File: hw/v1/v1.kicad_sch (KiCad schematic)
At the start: 0 parts

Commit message: Draw schematic for module V1
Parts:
- added J1: Expansion Output, symbol Connector:Conn_01x05_Socket
- added J2: Expansion Input, symbol Connector:Conn_01x05_Pin
- added U1, U2, U3: Common Anode, Display_7Segment:CA56-12CGKWA, symbol Display_Character:CA56-12CGKWA
- added U4, U5, U6: 74HC595, symbol 74xx:74HC595
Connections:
- new net: U5.9 (QH'), U6.14 (SER)
- new net: U4.9 (QH'), U5.14 (SER)
- new net +5V: J1.1 (Pin_1), J2.1 (Pin_1), U4.10 (~{SRCLR}), U4.16 (VCC), U5.10 (~{SRCLR}), U5.16 (VCC), U6.10 (~{SRCLR}), U6.16 (VCC)
- new net CLOCK: J1.3 (Pin_3), J2.3 (Pin_3), U4.11 (SRCLK), U5.11 (SRCLK), U6.11 (SRCLK)
- new net D1_SEG1: U1.12 (CA1)
- new net D1_SEG2: U1.9 (CA2)
- new net D1_SEG3: U1.8 (CA3), U5.2 (QC)
- new net D1_SEG4: U1.6 (CA4), U5.3 (QD)
- new net D2_SEG1: U2.12 (CA1), U5.4 (QE)
- new net D2_SEG2: U2.9 (CA2)
- new net D2_SEG3: U2.8 (CA3)
- new net D2_SEG4: U2.6 (CA4)
- new net D3_SEG1: U3.12 (CA1), U6.15 (QA)
- new net D3_SEG2: U3.9 (CA2), U6.1 (QB)
- new net D3_SEG3: U3.8 (CA3), U6.2 (QC)
- new net D3_SEG4: U3.6 (CA4), U6.3 (QD)
- new net DATA_IN: J2.2 (Pin_2), U4.14 (SER)
- new net DATA_OUT: J1.2 (Pin_2), U6.9 (QH')
- new net GND: J1.5 (Pin_5), J2.5 (Pin_5), U4.13 (~{OE}), U4.8 (GND), U5.13 (~{OE}), U5.8 (GND), U6.13 (~{OE}), U6.8 (GND)
- new net LATCH: J1.4 (Pin_4), J2.4 (Pin_4), U4.12 (RCLK), U5.12 (RCLK), U6.12 (RCLK)
- new net SEG_A: U1.11 (a), U2.11 (a), U4.15 (QA)
- new net SEG_B: U1.7 (b), U4.1 (QB)
- new net SEG_C: U1.4 (c), U2.4 (c)
- new net SEG_D: U1.2 (d), U2.2 (d), U3.2 (d)
- new net SEG_DP: U3.3 (DPX)
- new net SEG_E: U1.1 (e), U2.1 (e)
- new net SEG_F: U1.10 (f), U2.10 (f), U3.10 (f)
- new net SEG_G: U1.5 (g), U3.5 (g)
- no-connect marks 0 -> 4
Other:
- note added: "Expansion Headers"
- note added: "Seven Segment Modules"
- note added: "Shift Registers"
- company: (none) -> DIY Laboratories
- title: (none) -> 4x3 Seven Seven Segment Module

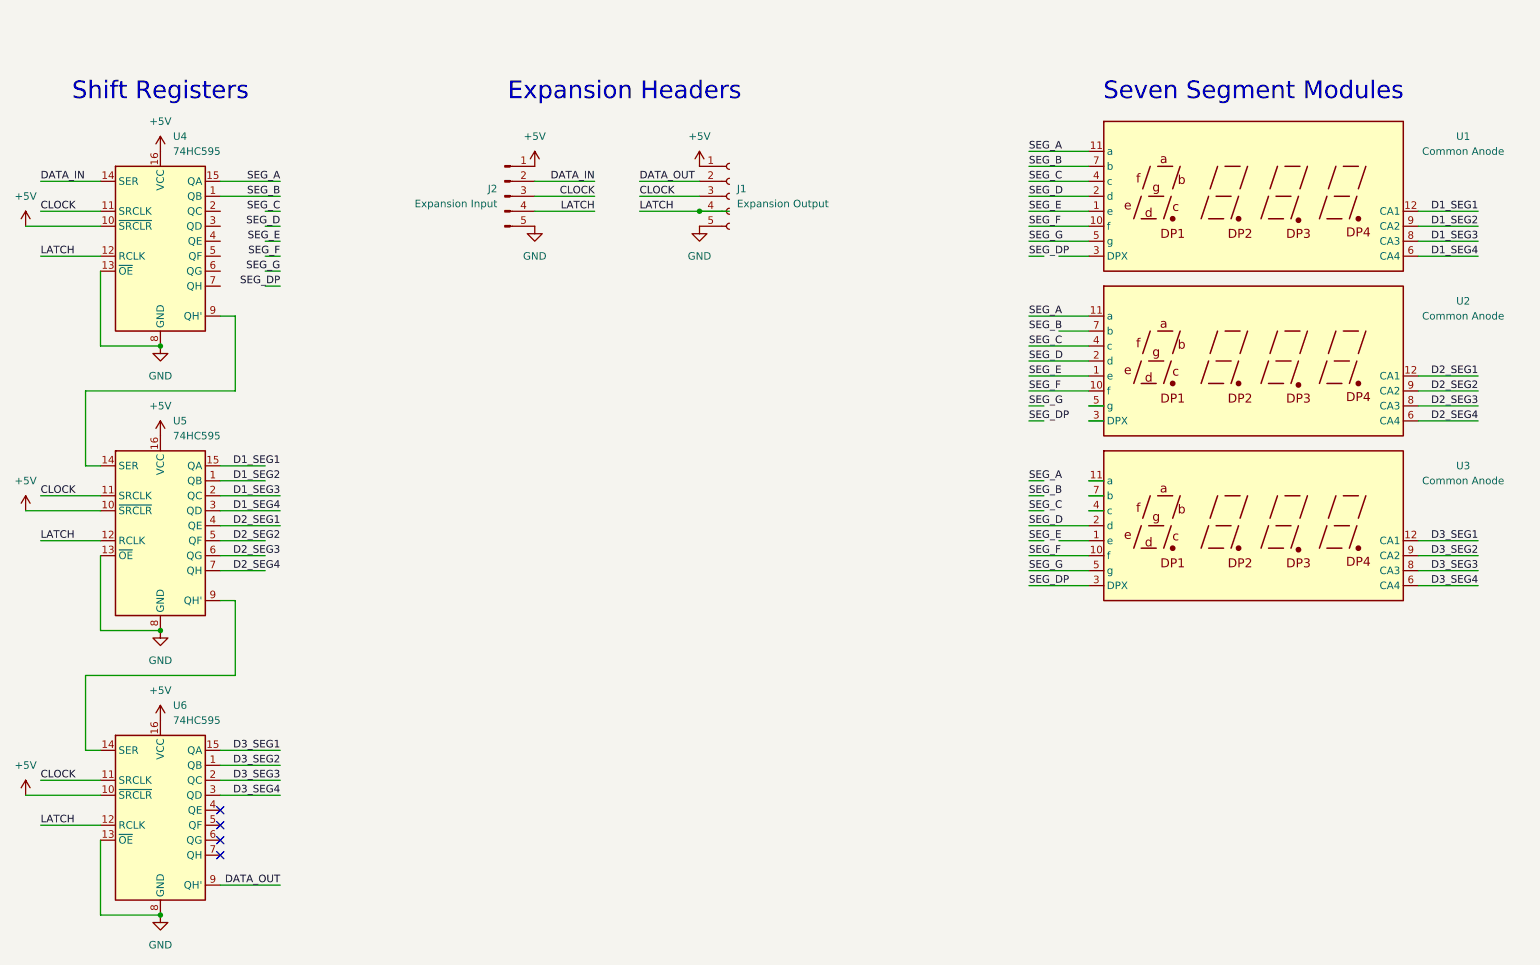
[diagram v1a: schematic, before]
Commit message: Add resistors to segment pins, create table for shift register outputs
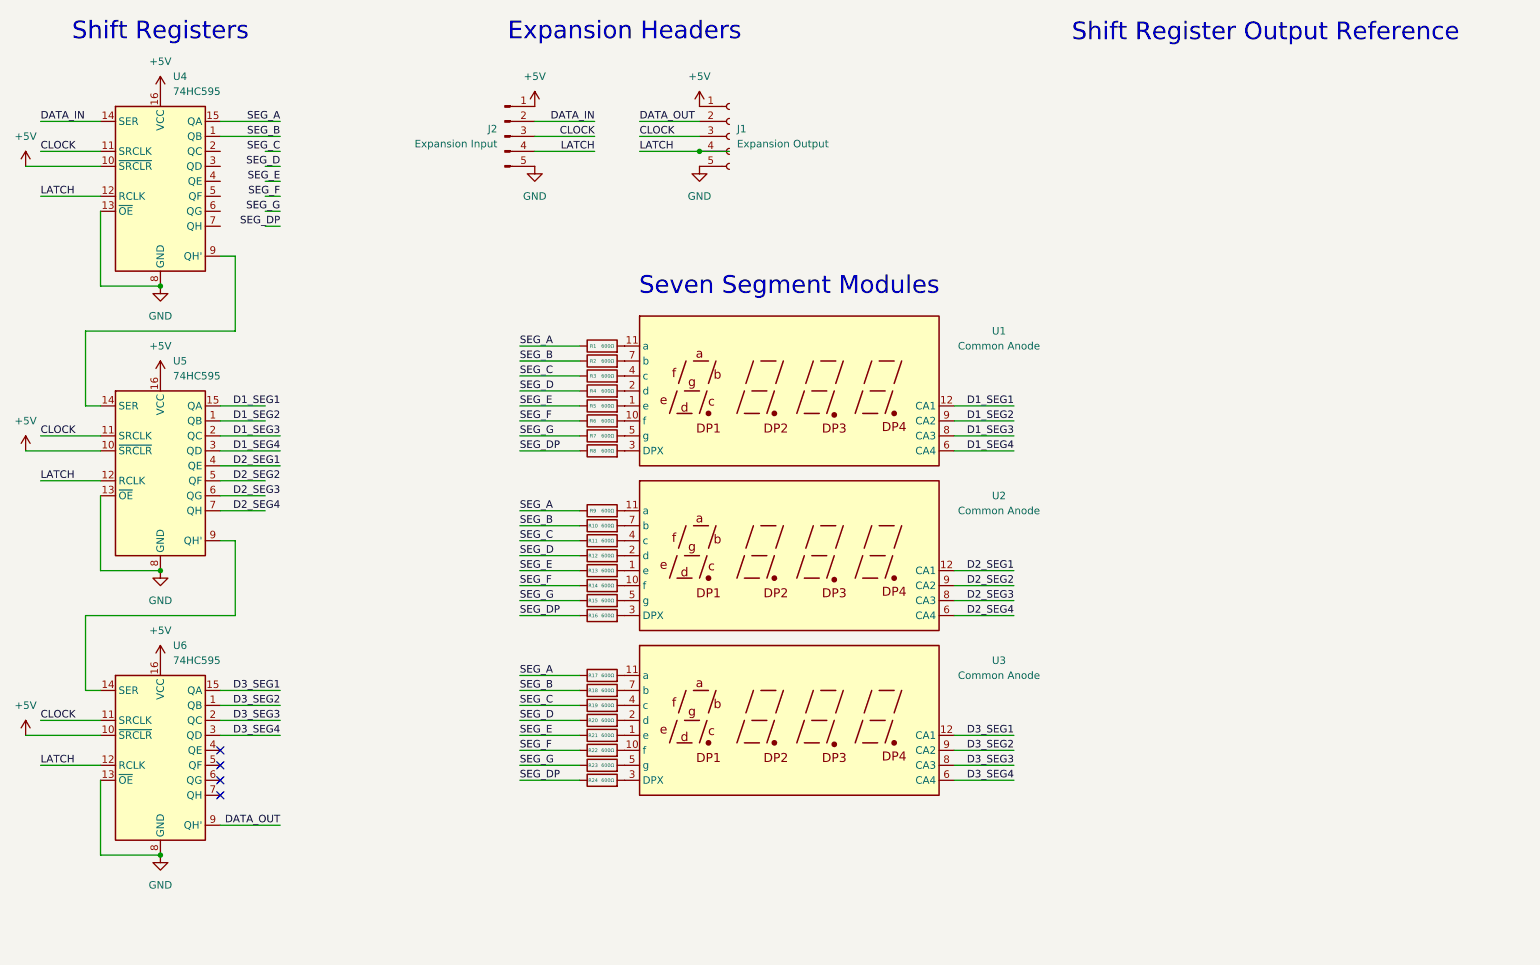
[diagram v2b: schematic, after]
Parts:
- added R1, R10, R11, R12, R13, R14, R15, R16, R17, R18, R19, R2, R20, R21, R22, R23, R24, R3, R4, R5, R6, R7, R8, R9: 600Ω, symbol Device:R
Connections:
- net SEG_A: now also R1.1, R17.1, R9.1; no longer U1.11 (a), U2.11 (a)
- net SEG_B: now also R10.1, R18.1, R2.1; no longer U1.7 (b)
- net SEG_C: now also R11.1, R19.1, R3.1; no longer U1.4 (c), U2.4 (c)
- net SEG_D: now also R12.1, R20.1, R4.1; no longer U1.2 (d), U2.2 (d), U3.2 (d)
- net SEG_DP: now also R16.1, R24.1, R8.1; no longer U3.3 (DPX)
- net SEG_E: now also R13.1, R21.1, R5.1; no longer U1.1 (e), U2.1 (e)
- net SEG_F: now also R14.1, R22.1, R6.1; no longer U1.10 (f), U2.10 (f), U3.10 (f)
- net SEG_G: now also R15.1, R23.1, R7.1; no longer U1.5 (g), U3.5 (g)
- net at U1.3 (DPX): now also R8.2
- net at U2.3 (DPX): now also R16.2
- net at U2.5 (g): now also R15.2
- net at U2.7 (b): now also R10.2
- net at U3.1 (e): now also R21.2
- net at U3.11 (a): now also R17.2
- net at U3.4 (c): now also R19.2
- net at U3.7 (b): now also R18.2
- new net: R5.2, U1.1 (e)
- new net: R22.2, U3.10 (f)
- new net: R23.2, U3.5 (g)
- new net: R20.2, U3.2 (d)
- new net: R2.2, U1.7 (b)
- new net: R12.2, U2.2 (d)
- new net: R9.2, U2.11 (a)
- new net: R14.2, U2.10 (f)
- new net: R3.2, U1.4 (c)
- new net: R6.2, U1.10 (f)
- new net: R1.2, U1.11 (a)
- new net: R4.2, U1.2 (d)
- new net: R7.2, U1.5 (g)
- new net: R13.2, U2.1 (e)
- new net: R11.2, U2.4 (c)
- new net: R24.2, U3.3 (DPX)
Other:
- note added: "Shift Register Output Reference"
- moved on the sheet: J1, J2, U1, U2, U3, U4, U5, U6
